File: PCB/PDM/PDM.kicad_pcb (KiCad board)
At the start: 2 copper layers, 141 parts, among them IC1 BTS70021EPPXUMA1, IC10 BTS70021EPPXUMA1, IC11 BTS70021EPPXUMA1, IC12 LM5050MK-1_NOPB, IC13 LM5050MK-1_NOPB, IC14 TLE8104E, IC2 BTS70021EPPXUMA1, IC3 BTS500101TAEATMA1, IC4 TS5A21366DCUR, IC5 TMP126NDCKR, IC6 TMP126NDCKR, IC7 BTS722204ESAXUMA1, IC8 BTS722204ESAXUMA1, IC9 BTS500101TAEATMA1, Q1 MMBT3904, Q2 IAUA250N04S6N007AUMA1, Q3 IAUA250N04S6N007AUMA1, U1 STM32L496VGTx, U2 MCP2561-E-SN, U3 MCP2561-E-SN

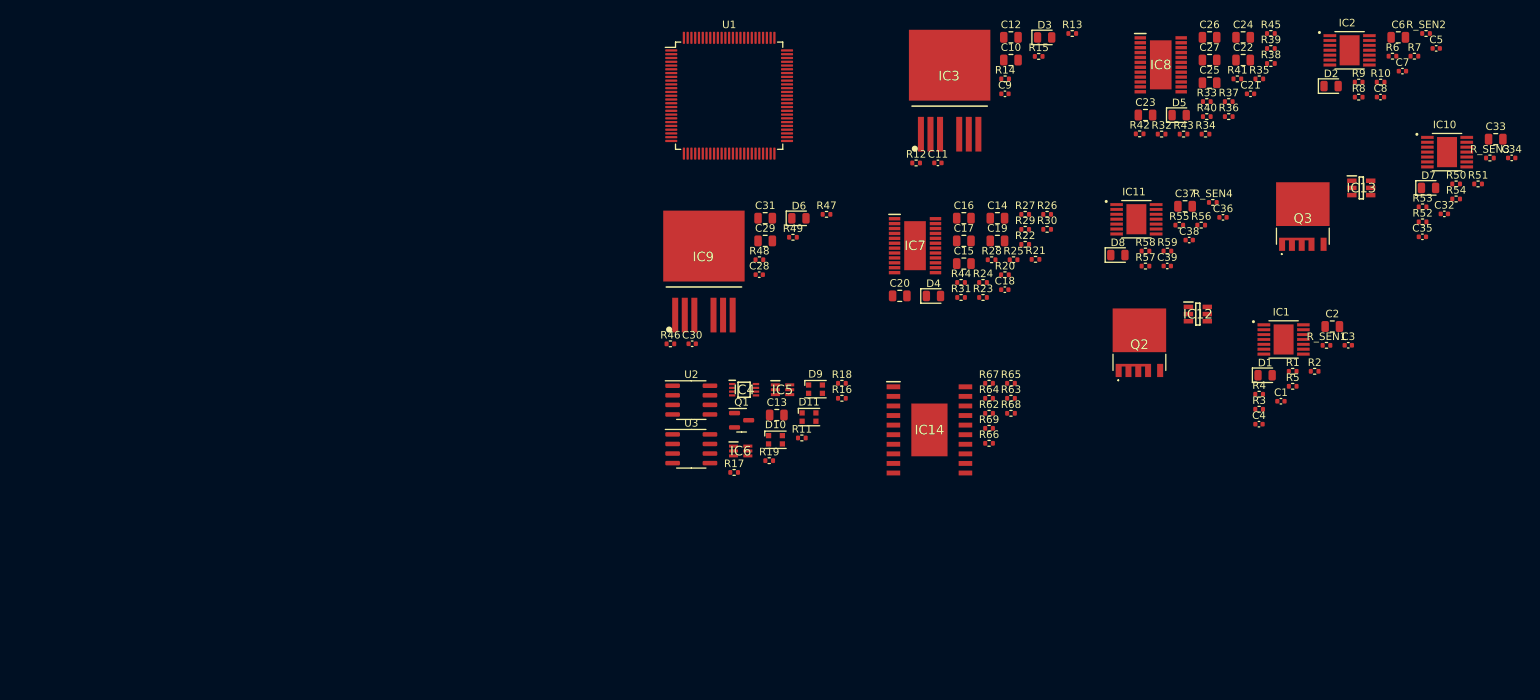
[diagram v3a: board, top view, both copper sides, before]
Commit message: Concept revision and MCU section changes
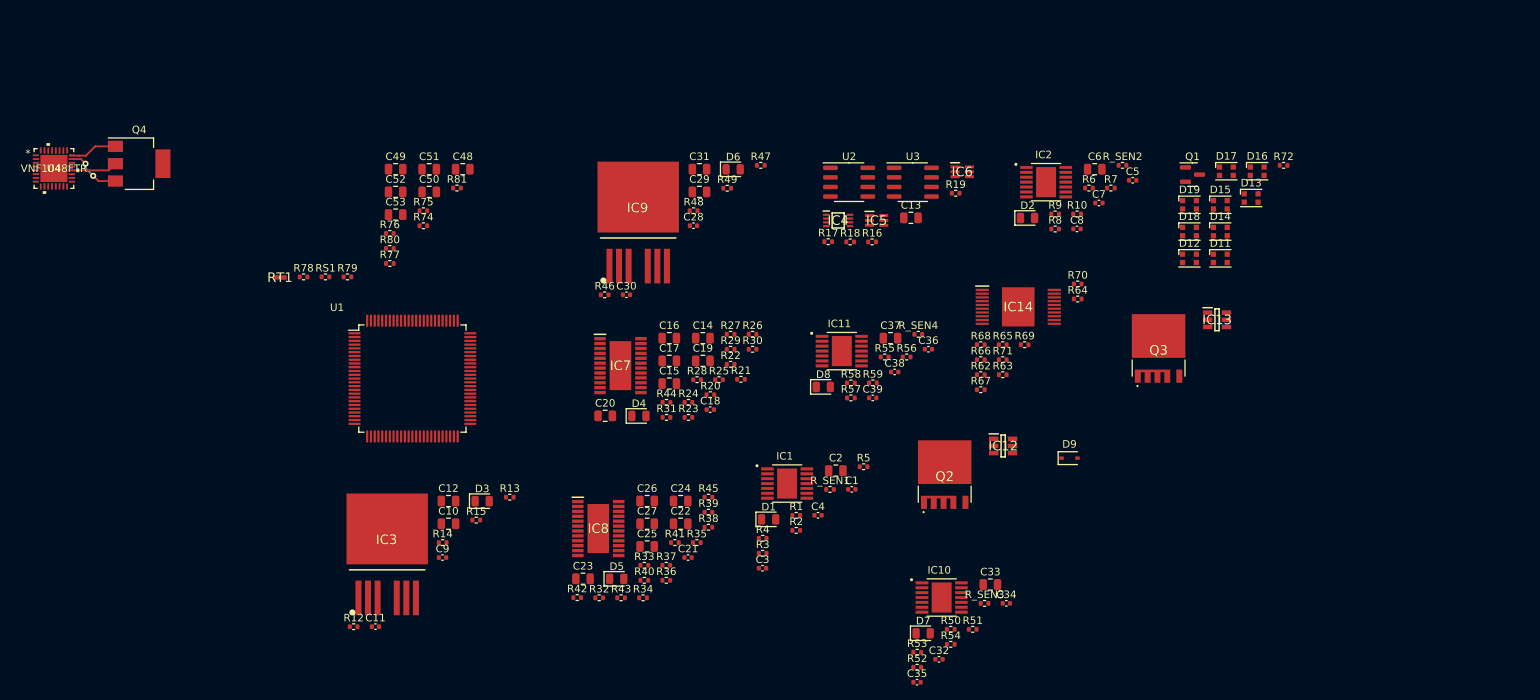
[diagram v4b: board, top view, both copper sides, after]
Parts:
- removed D10: WS2812B, LED_SMD:LED_WS2812B-2020_PLCC4_2.0x2.0mm
- removed R11: 1k, Resistor_SMD:R_0402_1005Metric
- added C48: 1uF, Capacitor_SMD:C_0805_2012Metric, F.Cu at (138.4, 49.0)
- added C49: 470nF, Capacitor_SMD:C_0805_2012Metric, F.Cu at (129.5, 49.0)
- added C50: 470nF, Capacitor_SMD:C_0805_2012Metric, F.Cu at (134.0, 52.0)
- added C51: 470nF, Capacitor_SMD:C_0805_2012Metric, F.Cu at (134.0, 49.0)
- added C52: 20uF, Capacitor_SMD:C_0805_2012Metric, F.Cu at (129.5, 52.0)
- added C53: 100nF, Capacitor_SMD:C_0805_2012Metric, F.Cu at (129.5, 55.0)
- added D12: WS2812B, LED_SMD:LED_WS2812B-2020_PLCC4_2.0x2.0mm, F.Cu at (234.8, 60.8)
- added D13: WS2812B, LED_SMD:LED_WS2812B-2020_PLCC4_2.0x2.0mm, F.Cu at (242.9, 52.8)
- added D14: WS2812B, LED_SMD:LED_WS2812B-2020_PLCC4_2.0x2.0mm, F.Cu at (238.9, 57.3)
- added D15: WS2812B, LED_SMD:LED_WS2812B-2020_PLCC4_2.0x2.0mm, F.Cu at (238.9, 53.7)
- added D16: WS2812B, LED_SMD:LED_WS2812B-2020_PLCC4_2.0x2.0mm, F.Cu at (243.7, 49.3)
- added D17: WS2812B, LED_SMD:LED_WS2812B-2020_PLCC4_2.0x2.0mm, F.Cu at (239.7, 49.3)
- added D18: WS2812B, LED_SMD:LED_WS2812B-2020_PLCC4_2.0x2.0mm, F.Cu at (234.8, 57.3)
- added D19: WS2812B, LED_SMD:LED_WS2812B-2020_PLCC4_2.0x2.0mm, F.Cu at (234.8, 53.7)
- added Q4: NDT3055L, Package_TO_SOT_SMD:SOT-223-3_TabPin2, F.Cu at (95.5, 48.3)
- added R70: 1.2k, Resistor_SMD:R_0402_1005Metric, F.Cu at (219.9, 64.2)
- added R71: 1.2k, Resistor_SMD:R_0402_1005Metric, F.Cu at (210.0, 74.2)
- added R72: 1k, Resistor_SMD:R_0402_1005Metric, F.Cu at (247.2, 48.5)
- added R74: 1.2k, Resistor_SMD:R_0402_1005Metric, F.Cu at (133.2, 56.5)
- added R75: 1.2k, Resistor_SMD:R_0402_1005Metric, F.Cu at (133.2, 54.5)
- added R76: 1.2k, Resistor_SMD:R_0402_1005Metric, F.Cu at (128.7, 57.5)
- added R77: 1.2k, Resistor_SMD:R_0402_1005Metric, F.Cu at (128.7, 61.5)
- added R78: 1.2k, Resistor_SMD:R_0402_1005Metric, F.Cu at (117.3, 63.3)
- added R79: 1.2k, Resistor_SMD:R_0402_1005Metric, F.Cu at (123.1, 63.3)
- added R80: 10k, Resistor_SMD:R_0402_1005Metric, F.Cu at (128.7, 59.5)
- added R81: 47k, Resistor_SMD:R_0402_1005Metric, F.Cu at (137.6, 51.5)
- added RS1: 1m, Resistor_SMD:R_0402_1005Metric, F.Cu at (120.2, 63.3)
- added RT1: B57232V5103F360, PDM_Additional:THRMC1005X60N, F.Cu at (114.2, 63.4)
- added U4: VNF1048FTR, PDM_Additional:QFN32L_5x5_STM, F.Cu at (84.2, 48.9)
- D9: value WS2812B -> 5.1V; footprint LED_SMD:LED_WS2812B-2020_PLCC4_2.0x2.0mm -> Diode_SMD:D_SOD-323
- IC14: value TLE8104E -> TLE9104SHXUMA1; footprint PDM_Additional:SOIC127P1030X255-21N -> PDM_Additional:SOP50P1030X260-21N
- R62, R68, R69: value 1.2k -> 4.7k
- R64, R65, R66: value 4.7k -> 1.2k
- moved C23 96.7 mm to (154.4, 103.3)
- moved D5 96.7 mm to (158.8, 103.3)
- moved R12 96.7 mm to (123.9, 109.7)
- moved R13 96.7 mm to (144.6, 92.5)
- moved R14 96.7 mm to (135.7, 98.5)
- moved R32 96.7 mm to (156.5, 105.8)
- moved R42 96.7 mm to (153.6, 105.8)
- moved R43 96.7 mm to (159.4, 105.8)
- moved R45 96.7 mm to (171.0, 92.5)
- moved C10 96.7 mm to (136.5, 96.0)
- moved C11 96.7 mm to (126.8, 109.6)
- moved C12 96.7 mm to (136.5, 93.0)
- moved C21 96.7 mm to (168.3, 100.5)
- moved C22 96.7 mm to (167.3, 96.0)
- moved C24 96.7 mm to (167.3, 93.0)
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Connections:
- net /BTS70021EPP0/ADC renamed /ocp_concept1/BTS70021EPP0/ADC
- net /BTS70021EPP0/DEN renamed /ocp_concept1/BTS70021EPP0/DEN
- net /BTS70021EPP0/IN renamed /ocp_concept1/BTS70021EPP0/IN
- net /BTS70021EPP0/OUT renamed /ocp_concept1/BTS70021EPP0/OUT
- net /BTS70021EPP0/VS renamed /ocp_concept1/BTS70021EPP0/VS
- net /TLE8104E/IN0 renamed /TLE9104SH/MISO
- net /TLE8104E/IN1 renamed /TLE9104SH/IN2
- net /TLE8104E/IN2 renamed /TLE9104SH/MOSI
- net /TLE8104E/IN3 renamed /TLE9104SH/CSN
- net /TLE8104E/MOSI renamed /TLE9104SH/SCLK
- D11 pad 2: unconnected-(D11-Pad2) -> Net-(D11-Pad2)
- D11 pad 4: Net-(D10-Pad2) -> /user_peripheral/STATUS_LED_D
- D9 pad 1: +5V -> /ocp_concept1/SANALOG_1
- D9 pad 2: Net-(D10-Pad4) -> GND
- IC14 pad 1: GND -> Net-(C44-Pad2)
- IC14 pad 10: GND -> Net-(C45-Pad2)
- IC14 pad 11: GND -> Net-(C47-Pad2)
- IC14 pad 12: Net-(IC14-Pad12) -> GND
- IC14 pad 13: unconnected-(IC14-Pad13) -> Net-(IC14-Pad13)
- IC14 pad 14: unconnected-(IC14-Pad14) -> Net-(IC14-Pad14)
- IC14 pad 15: Net-(IC14-Pad15) -> +3.3V
- IC14 pad 16: Net-(IC14-Pad16) -> +5V
- IC14 pad 18: unconnected-(IC14-Pad18) -> Net-(IC14-Pad18)
- IC14 pad 19: Net-(IC14-Pad19) -> GND
- IC14 pad 2: Net-(IC14-Pad2) -> GND
- IC14 pad 20: GND -> Net-(C46-Pad2)
- IC14 pad 21: unconnected-(IC14-Pad21) -> GND
- IC14 pad 3: unconnected-(IC14-Pad3) -> Net-(IC14-Pad3)
- IC14 pad 4: unconnected-(IC14-Pad4) -> Net-(IC14-Pad4)
- IC14 pad 5: unconnected-(IC14-Pad5) -> Net-(IC14-Pad5)
- IC14 pad 7: unconnected-(IC14-Pad7) -> Net-(IC14-Pad7)
- IC14 pad 8: unconnected-(IC14-Pad8) -> Net-(IC14-Pad8)
- IC14 pad 9: Net-(IC14-Pad9) -> GND
- R62 pad 1: Net-(IC14-Pad6) -> /TLE9104SH/IN0
- R62 pad 2: /TLE8104E/CSN -> Net-(IC14-Pad3)
- R63 pad 2: Net-(IC14-Pad2) -> Net-(IC14-Pad4)
- R64 pad 2: Net-(IC14-Pad9) -> Net-(IC14-Pad5)
- R65 pad 2: Net-(IC14-Pad19) -> Net-(IC14-Pad6)
- R66 pad 2: Net-(IC14-Pad12) -> Net-(IC14-Pad7)
- R67 pad 1: Net-(IC14-Pad17) -> Net-(IC14-Pad8)
- R68 pad 1: Net-(IC14-Pad16) -> /TLE9104SH/IN1
- R68 pad 2: /TLE8104E/SCLK -> Net-(IC14-Pad18)
- R69 pad 1: Net-(IC14-Pad15) -> /TLE9104SH/IN3
- R69 pad 2: /TLE8104E/MISO -> Net-(IC14-Pad17)
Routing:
- net /VNF1048FTR/MOS_OUT: track 0.00 -> 7.33 mm, vias 0 -> 2
- net /VNF1048FTR/MOS_GATE: track 0.00 -> 6.51 mm
- net /VNF1048FTR/MOS_IN: track 0.00 -> 6.14 mm

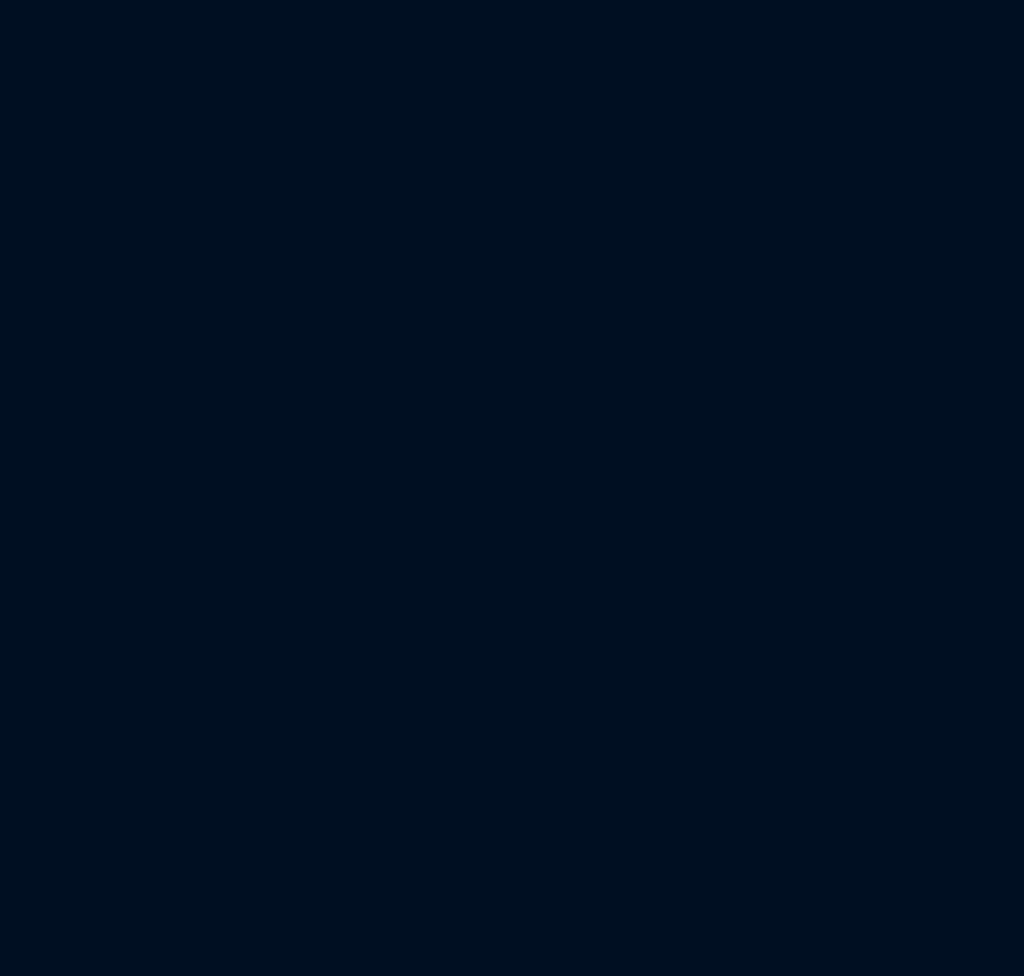
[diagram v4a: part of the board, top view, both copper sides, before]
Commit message: MCU preliminary scheme and qspi flash
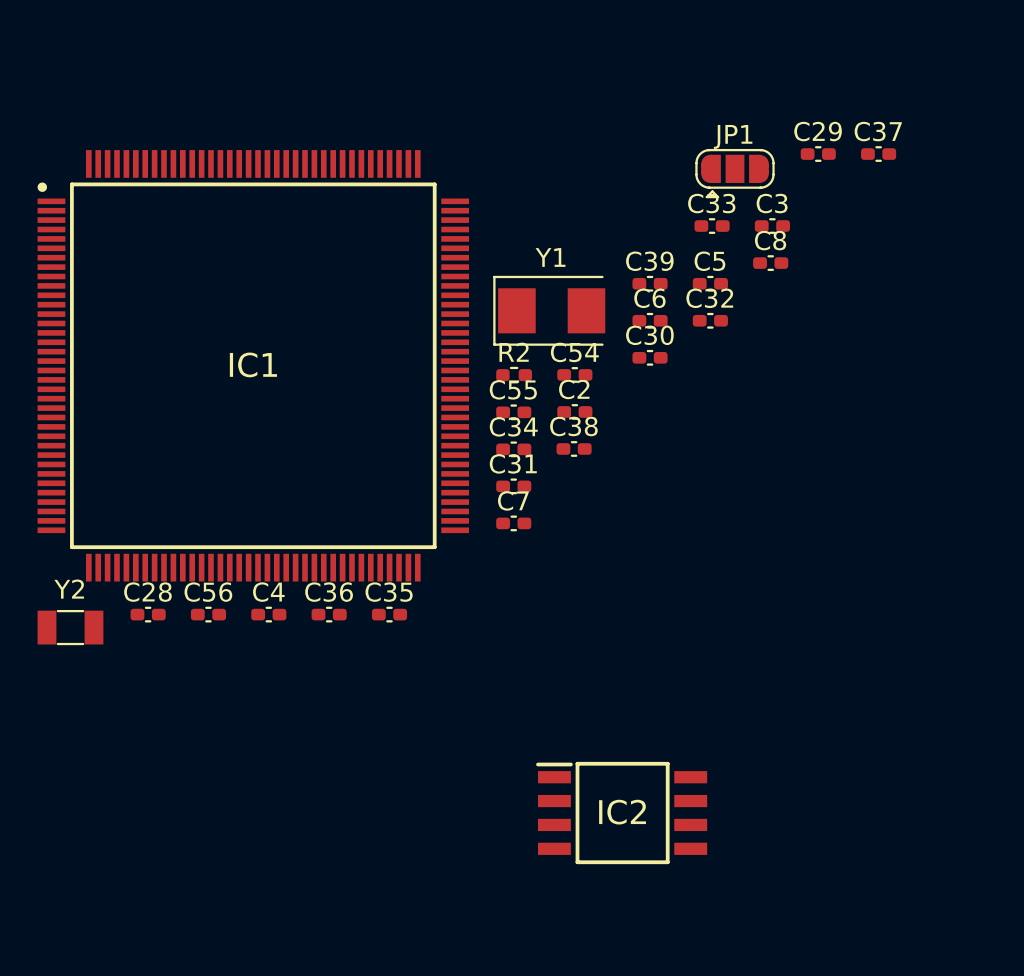
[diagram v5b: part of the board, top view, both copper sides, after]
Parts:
- added C2: 4u7, Capacitor_SMD:C_0402_1005Metric_Pad0.74x0.62mm_HandSolder, F.Cu at (92.5, 89.4)
- added C28: 100n, Capacitor_SMD:C_0402_1005Metric_Pad0.74x0.62mm_HandSolder, F.Cu at (69.8, 100.2)
- added C29: 100n, Capacitor_SMD:C_0402_1005Metric_Pad0.74x0.62mm_HandSolder, F.Cu at (105.4, 75.7)
- added C3: 10pF, Capacitor_SMD:C_0402_1005Metric_Pad0.74x0.62mm_HandSolder, F.Cu at (103.0, 79.5)
- added C30: 100n, Capacitor_SMD:C_0402_1005Metric_Pad0.74x0.62mm_HandSolder, F.Cu at (96.5, 86.5)
- added C31: 100n, Capacitor_SMD:C_0402_1005Metric_Pad0.74x0.62mm_HandSolder, F.Cu at (89.2, 93.4)
- added C32: 100n, Capacitor_SMD:C_0402_1005Metric_Pad0.74x0.62mm_HandSolder, F.Cu at (99.7, 84.6)
- added C33: 100n, Capacitor_SMD:C_0402_1005Metric_Pad0.74x0.62mm_HandSolder, F.Cu at (99.8, 79.5)
- added C34: 100n, Capacitor_SMD:C_0402_1005Metric_Pad0.74x0.62mm_HandSolder, F.Cu at (89.2, 91.4)
- added C35: 100n, Capacitor_SMD:C_0402_1005Metric_Pad0.74x0.62mm_HandSolder, F.Cu at (82.6, 100.2)
- added C36: 100n, Capacitor_SMD:C_0402_1005Metric_Pad0.74x0.62mm_HandSolder, F.Cu at (79.4, 100.2)
- added C37: 100n, Capacitor_SMD:C_0402_1005Metric_Pad0.74x0.62mm_HandSolder, F.Cu at (108.6, 75.7)
- added C38: 100n, Capacitor_SMD:C_0402_1005Metric_Pad0.74x0.62mm_HandSolder, F.Cu at (92.4, 91.4)
- added C39: 100n, Capacitor_SMD:C_0402_1005Metric_Pad0.74x0.62mm_HandSolder, F.Cu at (96.5, 82.6)
- added C4: 1u, Capacitor_SMD:C_0402_1005Metric_Pad0.74x0.62mm_HandSolder, F.Cu at (76.2, 100.2)
- added C5: 100n, Capacitor_SMD:C_0402_1005Metric_Pad0.74x0.62mm_HandSolder, F.Cu at (99.7, 82.6)
- added C54: 1u, Capacitor_SMD:C_0402_1005Metric_Pad0.74x0.62mm_HandSolder, F.Cu at (92.5, 87.4)
- added C55: 10pF, Capacitor_SMD:C_0402_1005Metric_Pad0.74x0.62mm_HandSolder, F.Cu at (89.2, 89.4)
- added C56: 10pF, Capacitor_SMD:C_0402_1005Metric_Pad0.74x0.62mm_HandSolder, F.Cu at (73.0, 100.2)
- added C6: 100n, Capacitor_SMD:C_0402_1005Metric_Pad0.74x0.62mm_HandSolder, F.Cu at (96.5, 84.6)
- added C7: 10pF, Capacitor_SMD:C_0402_1005Metric_Pad0.74x0.62mm_HandSolder, F.Cu at (89.2, 95.3)
- added C8: 100n, Capacitor_SMD:C_0402_1005Metric_Pad0.74x0.62mm_HandSolder, F.Cu at (102.9, 81.5)
- added IC1: STM32L496ZGT6, PDM_Additional:QFP50P2200X2200X160-144N, F.Cu at (75.4, 87.0)
- added IC2: AT25SF128A-SHB-T, PDM_Additional:SOIC127P798X216-8N, F.Cu at (95.0, 110.7)
- added JP1: SolderJumper_3_Open, Jumper:SolderJumper-3_P1.3mm_Open_RoundedPad1.0x1.5mm, F.Cu at (101.0, 76.5)
- added R2: 1k, Resistor_SMD:R_0402_1005Metric_Pad0.72x0.64mm_HandSolder, F.Cu at (89.2, 87.4)
- added Y1: 48Mhz, Crystal:Crystal_SMD_5032-2Pin_5.0x3.2mm, F.Cu at (91.2, 84.0)
- added Y2: 32KHz, Crystal:Crystal_SMD_3215-2Pin_3.2x1.5mm, F.Cu at (65.6, 100.9)
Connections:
- net +3.3V renamed VDD
